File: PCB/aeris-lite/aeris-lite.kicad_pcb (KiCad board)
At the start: 2 copper layers, 112 x 82 mm, 47 parts, among them J1 PMSA003A, J2 SHT45, J3 LPS22HB, J4 SCD40, J5 SGP41, J6 USB-C Input, J7 OUT, Q1 BSS138, Q2 BSS138, U1 ESP32-C6-SUPERMINI, U2 74AHCT244

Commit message: PCVB : Work in progress
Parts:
- removed H5: MountingHole, MountingHole:MountingHole_2.2mm_M2
- removed J1: PMSA003A, esp32-h2-supermini:PLANTOWER_PMSA003-A
- removed J2: SHT45, esp32-h2-supermini:SHT45-Breakout
- removed J3: LPS22HB, esp32-h2-supermini:LPS22HB-Breakout
- removed J4: SCD40, esp32-h2-supermini:SCD40-Breakout
- removed J5: SGP41, esp32-h2-supermini:SGP41-Breakout
- removed J7: OUT, Connector_PinHeader_2.54mm:PinHeader_1x03_P2.54mm_Vertical
- removed Q1, Q2: BSS138, Package_TO_SOT_SMD:SOT-23
- removed R10, R11, R12, R13: 47R, Resistor_SMD:R_0805_2012Metric
- removed R7, R8: 10K, Resistor_SMD:R_0805_2012Metric
- added C11: 100µF, Capacitor_SMD:CP_Elec_6.3x5.9, F.Cu at (78.1, 47.0)
- added C12: 0.1µF, Capacitor_SMD:C_0805_2012Metric, F.Cu at (100.5, 54.4)
- added C13: 0.1µF, Capacitor_SMD:C_0805_2012Metric, F.Cu at (136.3, 77.4)
- added C14: 0.1µF, Capacitor_SMD:C_0805_2012Metric, F.Cu at (118.5, 55.2)
- added C15: 1µF, Capacitor_SMD:C_0805_2012Metric, F.Cu at (119.6, 61.2)
- added C16: 1µF, Capacitor_SMD:C_0805_2012Metric, F.Cu at (117.0, 48.4)
- added Sen1: SCD4x, Sensor:Sensirion_SCD4x-1EP_10.1x10.1mm_P1.25mm_EP4.8x4.8mm, F.Cu at (103.8, 69.1)
- added U4: SHT4x, Sensor_Humidity:Sensirion_DFN-4_1.5x1.5mm_P0.8mm_SHT4x_NoCentralPad, F.Cu at (133.8, 86.5)
- added U6: DPS368XTSA1, DPS368XTSA1:XDCR_DPS368XTSA1, F.Cu at (75.5, 90.8)
- added U7: SGP41-D-R4, SGP41-D-R4:XDCR_SGP41-D-R4, F.Cu at (78.5, 72.5)
- C1, C4: footprint Capacitor_SMD:C_1206_3216Metric -> Capacitor_SMD:C_0805_2012Metric
- R1, R2: value 4.7K -> 10K
- R3: value 10K -> 330R
- R6: value 10K -> 4.7R
- R9: value 47R -> 470R
- U2: value 74AHCT244 -> 74AHC1G125; footprint Package_SO:SOIC-20W_7.5x12.8mm_P1.27mm -> Package_TO_SOT_SMD:SOT-23-5
- moved H2 117.6 mm to (37.9, 31.0), turned to 0 degrees
- moved H3 96.3 mm to (122.5, 91.8), turned to 0 degrees
- moved H1 80.9 mm to (38.9, 93.9), turned to 0 degrees
- moved C10 71.6 mm to (59.1, 71.2), turned to 180 degrees
- moved D1 67.6 mm to (72.3, 34.1), turned to 180 degrees
- moved R9 64.9 mm to (70.5, 39.2), turned to 90 degrees
- moved U2 62.1 mm to (55.4, 34.5)
- moved D3 61.8 mm to (91.8, 34.1), turned to 180 degrees
- moved C8 61.0 mm to (74.0, 39.2), turned to -90 degrees
- moved D2 58.5 mm to (82.2, 34.1), turned to 180 degrees
- moved C3 55.2 mm to (56.0, 90.0)
- moved R6 51.8 mm to (100.0, 89.2)
- moved C9 51.2 mm to (84.0, 39.2), turned to -90 degrees
- moved D0 50.1 mm to (47.2, 90.2)
- moved J6 48.1 mm to (38.5, 80.0), turned to 0 degrees
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- renumbered D5 to D3, D3 to D4, D4 to D5
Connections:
- D1 pad 1: unconnected-(D1-DOUT-Pad1) -> Net-(D1-DOUT)
- D2 pad 1: unconnected-(D2-DOUT-Pad1) -> Net-(D2-DOUT)
- D2 pad 3: Net-(D2-DIN) -> Net-(D1-DOUT)
- D3 pad 1: unconnected-(D5-DOUT-Pad1) (its old number) -> Net-(D3-DOUT)
- D3 pad 3: Net-(D5-DIN) -> Net-(D2-DOUT)
- D4 pad 1: unconnected-(D3-DOUT-Pad1) -> Net-(D4-DOUT)
- D4 pad 3: Net-(D3-DIN) -> Net-(D3-DOUT)
- D5 pad 3: Net-(D4-DIN) -> Net-(D4-DOUT)
- R1 pad 2: SDA -> SDA_0
- R2 pad 1: SCL -> SCL_0
- R3 pad 2: +3V3 -> Net-(R3-Pad2)
- R4 pad 1: GPIO19 -> +3V3
- R4 pad 2: +3V3 -> SDA_1
- R5 pad 1: +3V3 -> SCL_1
- R5 pad 2: GPIO0 -> +3V3
- R6 pad 1: +3V3 -> unconnected-(R6-Pad1)
- R6 pad 2: GPIO3 -> unconnected-(R6-Pad2)
- R9 pad 1: CO2 -> Net-(R9-Pad1)
- U1 pad 11: SCL -> unconnected-(U1-IO7-Pad11)
- U1 pad 12: SDA -> unconnected-(U1-IO6-Pad12)
- U1 pad 13: RX -> unconnected-(U1-IO5-Pad13)
- U1 pad 14: TX -> SCL_1
- U1 pad 15: GPIO3 -> SDA_1
- U1 pad 17: GPIO1 -> unconnected-(U1-IO1-Pad17)
- U1 pad 18: GPIO0 -> unconnected-(U1-IO0-Pad18)
- U1 pad 3: GPIO14 -> SDA_0
- U1 pad 4: GPIO15 -> SCL_0
- U1 pad 5: GPIO18 -> unconnected-(U1-IO18-Pad5)
- U1 pad 6: GPIO19 -> unconnected-(U1-IO19-Pad6)
- U1 pad 7: GPIO20 -> unconnected-(U1-IO20-Pad7)
- U2 pad 2: GPIO1 -> Net-(R3-Pad2)
- U2 pad 3: NOx -> GND
- U2 pad 4: GPIO18 -> Net-(R9-Pad1)
- U2 pad 5: unconnected-(U2-2Y1-Pad5) -> +5V
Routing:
- net +3V3: track 185.5 -> 54.3 mm, vias 6 -> 2
- net +5V: track 269.8 -> 139.4 mm, vias 12 -> 1
- net SDA: track 116.2 -> 0.00 mm
- net SCL: track 111.4 -> 0.00 mm
- net GPIO19: track 81.7 -> 0.00 mm, vias 4 -> 0
- net TX: track 69.0 -> 0.00 mm, vias 1 -> 0
- net GPIO2: track 74.5 -> 7.17 mm, vias 4 -> 0
- net RX: track 64.7 -> 0.00 mm, vias 1 -> 0
- net GPIO1: track 37.7 -> 0.00 mm
- net NOx: track 37.1 -> 0.00 mm
- net SCL_1: track 0.00 -> 35.4 mm
- net SDA_0: track 0.00 -> 35.3 mm
- net SDA_1: track 0.00 -> 32.4 mm
- net SCL_0: track 0.00 -> 32.0 mm
- net GPIO15: track 31.0 -> 0.00 mm, vias 2 -> 0
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- removed copper zone on B.Cu, net GND
- removed copper zone on F.Cu, net GND
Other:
- outline, holes or cut-outs redrawn
- board text added: "100µF"
- board text added: "1µF"
- board text added: "22µF"
- board text added: "330Ω"
- board text added: "470Ω"
- board text added: "74AHC1G125"
- board text added: "AERIS Lite - v1.0"
- board text added: "Status"
- board text removed: "1"
- board text removed: "10"
- board text removed: "2"
- board text removed: "3V3"
- board text removed: "4.7KΩ"
- board text removed: "47Ω"
- board text removed: "9"
- board text removed: "AERIS - v1.1"
- board text removed: "GND"
- board text removed: "HV"
- board text removed: "IO0"
- board text removed: "IO3"
- board text removed: "PM2.5"
- board text removed: "SCL"
- board text removed: "SDA"

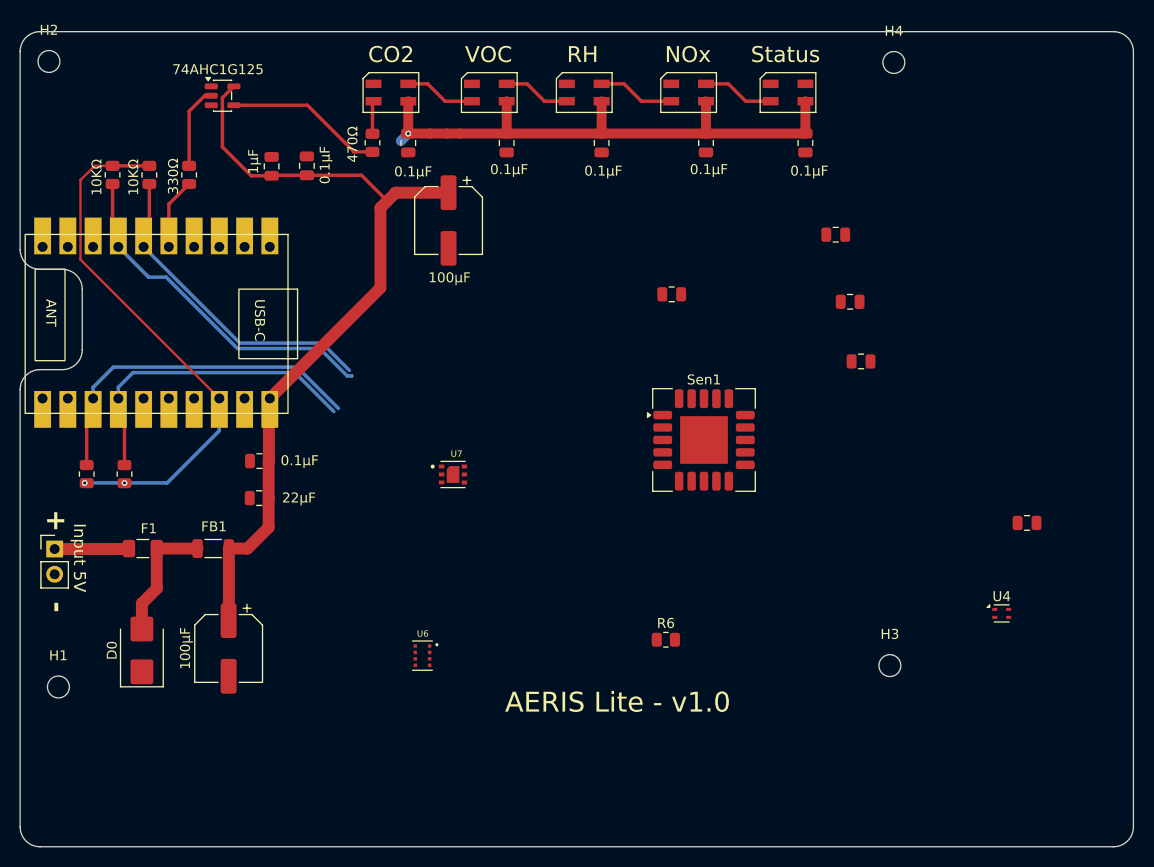
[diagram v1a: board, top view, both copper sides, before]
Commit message: feat: Implement fan control driver for Aeris_Lite
- Added fan_control.c and fan_control.h to manage PWM speed control and RPM monitoring for a 5V 4-wire PWM fan.
- Integrated GPIO configuration for fan power control and tachometer pulse counting.
- Implemented functions for initializing the fan system, setting power and speed, retrieving RPM, and checking fan status.
- Added adaptive control based on temperature and air quality sensor readings.
- Defined fan operating modes and status structure for better management and monitoring.
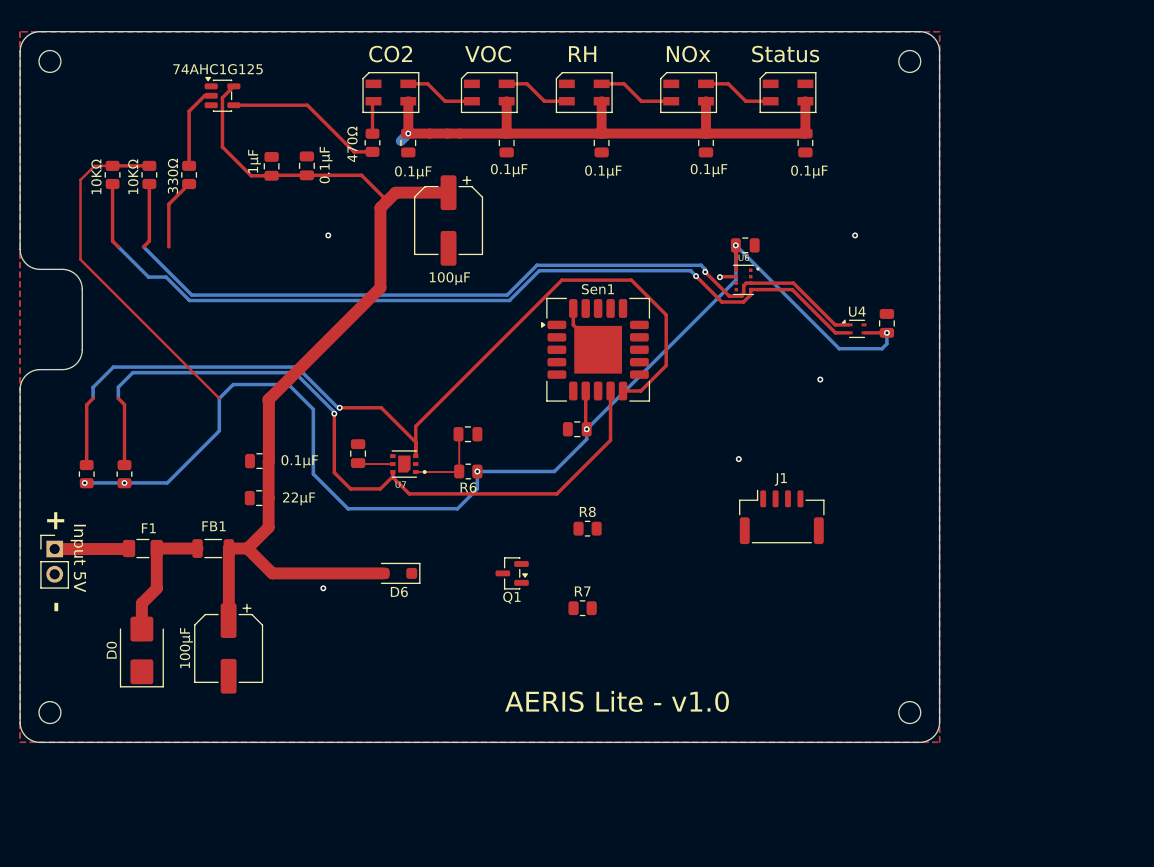
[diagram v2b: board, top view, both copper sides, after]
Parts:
- removed U1: ESP32-C6-SUPERMINI, esp32-h2-supermini:ESP32C6-Supermini
- added D6: N5819HW1-7-F, Diode_SMD:D_SOD-123F, F.Cu at (73.0, 82.5)
- added J1: Conn_01x04, Connector_JST:JST_GH_SM04B-GHS-TB_1x04-1MP_P1.25mm_Horizontal, F.Cu at (111.6, 76.8)
- added Q1: IRLML6344TRPBF, Package_TO_SOT_SMD:SOT-23, F.Cu at (84.5, 82.5)
- added R7: 1K, Resistor_SMD:R_0805_2012Metric, F.Cu at (91.6, 86.0)
- added R8: 10K, Resistor_SMD:R_0805_2012Metric, F.Cu at (92.1, 78.0)
- moved C16 52.9 mm to (69.0, 70.5), turned to 90 degrees
- moved U6 49.7 mm to (107.8, 53.0)
- moved C13 46.2 mm to (91.0, 68.0), turned to 180 degrees
- moved C15 40.2 mm to (80.0, 68.5)
- moved U4 32.1 mm to (119.2, 57.9)
- moved R6 26.1 mm to (80.1, 72.2), turned to 180 degrees
- moved Sen1 14.0 mm to (93.2, 60.0)
- moved C12 8.89 mm to (108.0, 49.5)
- moved H3 5.13 mm to (124.5, 96.5)
- moved U7 5.01 mm to (73.7, 71.5), turned to 180 degrees
- moved C14 4.29 mm to (122.2, 57.4), turned to 90 degrees
- moved H1 2.71 mm to (38.0, 96.5)
- moved H4 1.60 mm to (124.5, 31.0)
- moved H2 0.10 mm to (38.0, 31.0)
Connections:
- C12 pad 1: +3V3 -> GPIO7
- C13 pad 1: +3V3 -> GPIO7
- C14 pad 1: +3V3 -> GPIO7
- C15 pad 1: +3V3 -> Net-(U7-VDD)
- C16 pad 1: unconnected-(C16-Pad1) -> Net-(U7-VDD)
- C16 pad 2: unconnected-(C16-Pad2) -> GND
- R1 pad 1: +3V3 -> GPIO7
- R2 pad 2: +3V3 -> GPIO7
- R4 pad 1: +3V3 -> GPIO7
- R5 pad 2: +3V3 -> GPIO7
- R6 pad 1: unconnected-(R6-Pad1) -> GPIO7
- R6 pad 2: unconnected-(R6-Pad2) -> Net-(U7-VDD)
- Sen1 pad 7: +3V3 -> GPIO7
- U4 pad 3: +3V3 -> GPIO7
- U6 pad 8: +3V3 -> GPIO7
- U7 pad 1: +3V3 -> Net-(U7-VDD)
- U7 pad 4: unconnected-(U7-N/A-Pad4) -> GND
- U7 pad 5: unconnected-(U7-VDDH-Pad5) -> Net-(U7-VDD)
- U7 pad 7: unconnected-(U7-EXP-Pad7) -> GND
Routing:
- net GPIO7: track 0.00 -> 159.8 mm, vias 0 -> 6
- net SDA_0: track 35.3 -> 92.0 mm, vias 0 -> 1
- net +3V3: track 54.3 -> 0.00 mm, vias 2 -> 0
- net SDA_1: track 32.4 -> 85.0 mm, vias 0 -> 1
- net SCL_1: track 35.4 -> 87.5 mm, vias 0 -> 1
- net SCL_0: track 32.0 -> 76.0 mm, vias 0 -> 1
- net +5V: track 139.4 -> 154.2 mm
- net Net-(U7-VDD): track 0.00 -> 11.7 mm
- net GND: track 0.00 -> 6.86 mm, vias 0 -> 6
- added copper zone on B.Cu, net GND
- added copper zone on F.Cu, net GND
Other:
- board size 112 x 82 mm -> 92.5 x 71.5 mm
